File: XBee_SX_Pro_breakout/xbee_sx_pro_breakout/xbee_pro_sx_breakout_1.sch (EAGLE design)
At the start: 0 parts

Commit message: finished xbee library
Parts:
- added U$1: XBEE_SX_PRO, xbee_sx_pro:XBEE_SX_PRO
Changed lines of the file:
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@@
 </classes>
 <parts>
+<part name="U$1" library="xbee_sx_pro" deviceset="XBEE_SX_PRO" device=""/>
 </parts>
 <sheets>
@@
 </plain>
 <instances>
+<instance part="U$1" gate="G$1" x="53.34" y="33.02" smashed="yes"/>
 </instances>
 <busses>

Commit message: updated board
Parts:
- added J1: (no value), SparkFun-Connectors:CONN_08"
- added J2: (no value), SparkFun-Connectors:CONN_14
- added J3: (no value), SparkFun-Connectors:CONN_16
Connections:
- new net N$1: J3.1, U$1.NC
- new net N$10: J3.10, U$1.DIO5
- new net N$11: J3.11, U$1.VREF/NC
- new net N$12: J3.12, U$1.DIO9/ON/SLEEP
- new net N$13: J3.13, U$1.DIO7
- new net N$14: J3.14, U$1.DIO4
- new net N$15: J3.15, U$1.NC@6
- new net N$16: J3.16, U$1.GND@3
- new net N$17: J1.1, U$1.NC@5
- new net N$18: J1.2, U$1.NC@4
- new net N$19: J1.3, U$1.NC@3
- new net N$2: J3.2, U$1.RF_PAD
- new net N$20: J1.4, U$1.NC@2
- new net N$21: J1.5, U$1.DIO15/SPI_MISO
- new net N$22: J1.6, U$1.DIO16/SPI_MOSI
- new net N$23: J1.7, U$1.DIO17/SPI_SS
- new net N$24: J1.8, U$1.DIO18/SPI_CLK
- new net N$25: J2.1, U$1.GND@2
- new net N$26: J2.2, U$1.DIO19
- new net N$27: J2.3, U$1.GND@1
- new net N$28: J2.4, U$1.DIO8
- new net N$29: J2.5, U$1.NC@1
- new net N$3: J3.3, U$1.GND@4
- new net N$30: J2.6, U$1.DIO11
- new net N$31: J2.7, U$1.DIO10
- new net N$32: J2.8, U$1.RESET
- new net N$33: J2.9, U$1.DIO12
- new net N$34: J2.10, U$1.DIO14/DIN/CONFIG
- new net N$35: J2.11, U$1.DIO13/DOUT
- new net N$36: J2.12, U$1.VCC
- new net N$37: J2.13, U$1.GND@0
- new net N$38: J2.14, U$1.GND@5
- new net N$4: J3.4, U$1.NC@7
- new net N$5: J3.5, U$1.DIO0/AD0
- new net N$6: J3.6, U$1.DIO1/AD1
- new net N$7: J3.7, U$1.DIO2/AD2
- new net N$8: J3.8, U$1.DIO3/AD3
- new net N$9: J3.9, U$1.DIO6

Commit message: finished breakout board
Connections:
- net N$38 renamed GND
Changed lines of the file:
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@@
 </segment>
 </net>
-<net name="N$38" class="0">
+<net name="GND" class="0">
 <segment>
 <pinref part="U$1" gate="G$1" pin="GND@5"/>

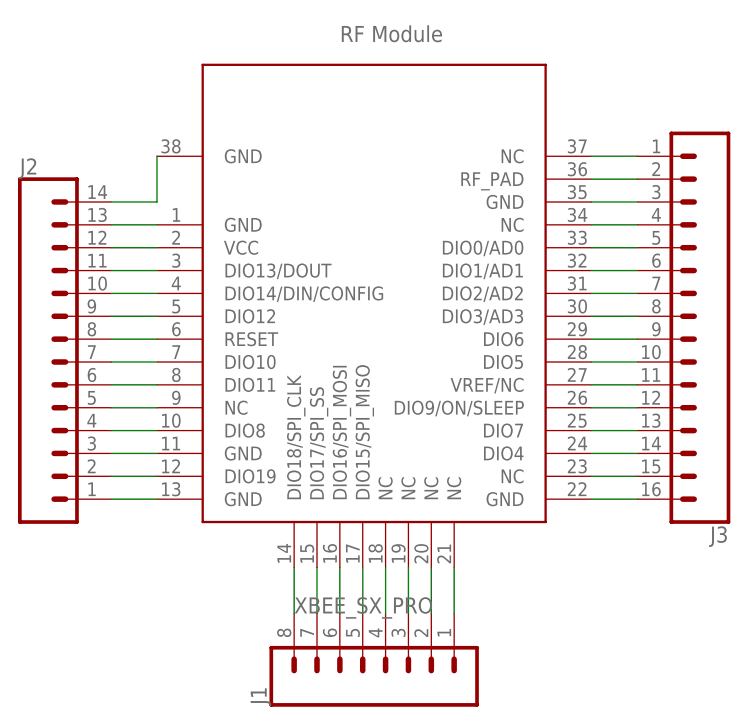
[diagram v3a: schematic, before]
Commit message: updated gnd signals
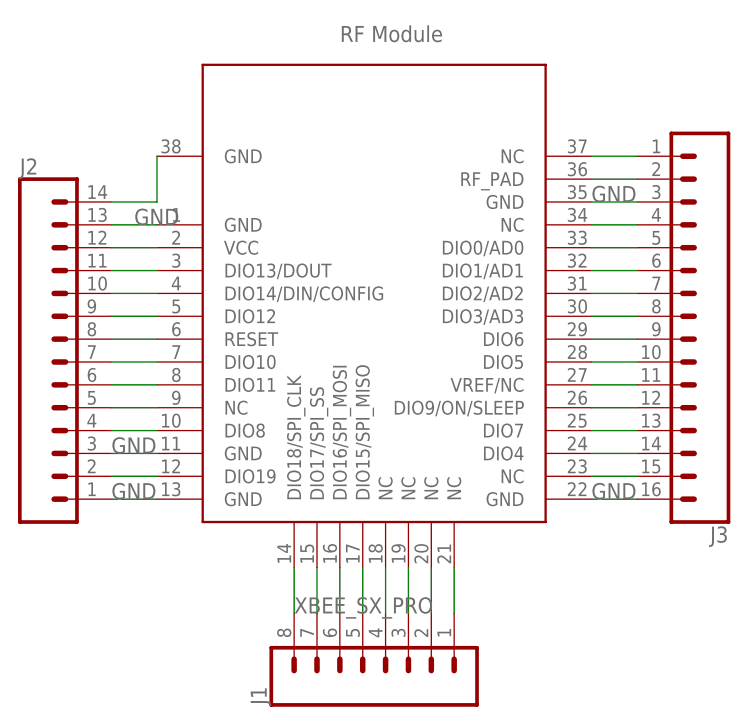
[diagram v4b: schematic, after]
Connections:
- net N$36 renamed VCC
- removed net N$16: J3.16, U$1.GND@3
- removed net N$25: J2.1, U$1.GND@2
- removed net N$27: J2.3, U$1.GND@1
- removed net N$3: J3.3, U$1.GND@4
- removed net N$37: J2.13, U$1.GND@0
- net GND: now also J2.1, J2.13, J2.3, J3.16, J3.3, U$1.GND@0, U$1.GND@1, U$1.GND@2, U$1.GND@3, U$1.GND@4
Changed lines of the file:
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@@
 </class>
 </classes>
+<modules>
+<module name="BREAKOUT" prefix="" dx="30.48" dy="20.32">
+<ports>
+</ports>
+<variantdefs>
+</variantdefs>
+<parts>
+</parts>
+<sheets>
+<sheet>
+<plain>
+</plain>
+<instances>
+</instances>
+<busses>
+</busses>
+<nets>
+</nets>
+</sheet>
+</sheets>
+</module>
+</modules>
 <parts>
 <part name="U$1" library="xbee_sx_pro" deviceset="XBEE_SX_PRO" device=""/>
@@
 </segment>
 </net>
-<net name="N$3" class="0">
-<segment>
-<pinref part="U$1" gate="G$1" pin="GND@4"/>
-<pinref part="J3" gate="G$1" pin="3"/>
-<wire x1="101.6" y1="71.12" x2="96.52" y2="71.12" width="0.1524" layer="91"/>
-</segment>
-</net>
 <net name="N$4" class="0">
 <segment>
@@
 </segment>
 </net>
-<net name="N$16" class="0">
-<segment>
-<pinref part="U$1" gate="G$1" pin="GND@3"/>
-<pinref part="J3" gate="G$1" pin="16"/>
-<wire x1="101.6" y1="38.1" x2="96.52" y2="38.1" width="0.1524" layer="91"/>
-</segment>
-</net>
 <net name="N$17" class="0">
 <segment>
@@
 </segment>
 </net>
-<net name="N$25" class="0">
-<segment>
-<pinref part="U$1" gate="G$1" pin="GND@2"/>
-<pinref part="J2" gate="G$1" pin="1"/>
-<wire x1="43.18" y1="38.1" x2="48.26" y2="38.1" width="0.1524" layer="91"/>
-</segment>
-</net>
 <net name="N$26" class="0">
 <segment>
@@
 </segment>
 </net>
-<net name="N$27" class="0">
-<segment>
-<pinref part="U$1" gate="G$1" pin="GND@1"/>
-<pinref part="J2" gate="G$1" pin="3"/>
-<wire x1="43.18" y1="43.18" x2="48.26" y2="43.18" width="0.1524" layer="91"/>
-</segment>
-</net>
 <net name="N$28" class="0">
 <segment>
@@
 </segment>
 </net>
-<net name="N$36" class="0">
+<net name="VCC" class="0">
 <segment>
 <pinref part="U$1" gate="G$1" pin="VCC"/>
 <pinref part="J2" gate="G$1" pin="12"/>
 <wire x1="43.18" y1="66.04" x2="48.26" y2="66.04" width="0.1524" layer="91"/>
-</segment>
-</net>
-<net name="N$37" class="0">
-<segment>
-<pinref part="U$1" gate="G$1" pin="GND@0"/>
-<pinref part="J2" gate="G$1" pin="13"/>
-<wire x1="43.18" y1="68.58" x2="48.26" y2="68.58" width="0.1524" layer="91"/>
 </segment>
 </net>
@@
 <wire x1="48.26" y1="71.12" x2="43.18" y2="71.12" width="0.1524" layer="91"/>
 </segment>
-</net>
+<segment>
+<pinref part="U$1" gate="G$1" pin="GND@2"/>
+<pinref part="J2" gate="G$1" pin="1"/>
+<wire x1="43.18" y1="38.1" x2="48.26" y2="38.1" width="0.1524" layer="91"/>
+<label x="43.18" y="38.1" size="1.778" layer="95"/>
+</segment>
+<segment>
+<pinref part="U$1" gate="G$1" pin="GND@0"/>
+<pinref part="J2" gate="G$1" pin="13"/>
+<wire x1="43.18" y1="68.58" x2="48.26" y2="68.58" width="0.1524" layer="91"/>
+<label x="45.72" y="68.58" size="1.778" layer="95"/>
+</segment>
+<segment>
+<pinref part="U$1" gate="G$1" pin="GND@3"/>
+<pinref part="J3" gate="G$1" pin="16"/>
+<wire x1="101.6" y1="38.1" x2="96.52" y2="38.1" width="0.1524" layer="91"/>
+<label x="96.52" y="38.1" size="1.778" layer="95"/>
+</segment>
+<segment>
+<pinref part="U$1" gate="G$1" pin="GND@4"/>
+<pinref part="J3" gate="G$1" pin="3"/>
+<wire x1="101.6" y1="71.12" x2="96.52" y2="71.12" width="0.1524" layer="91"/>
+<label x="96.52" y="71.12" size="1.778" layer="95"/>
+</segment>
+<segment>
+<pinref part="U$1" gate="G$1" pin="GND@1"/>
+<pinref part="J2" gate="G$1" pin="3"/>
+<wire x1="43.18" y1="43.18" x2="48.26" y2="43.18" width="0.1524" layer="91"/>
+<label x="43.18" y="43.18" size="1.778" layer="95"/>
+</segment>
+</net>
